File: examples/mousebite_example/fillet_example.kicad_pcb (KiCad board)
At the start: 4 copper layers, 43.2 x 30.5 mm, 0 parts

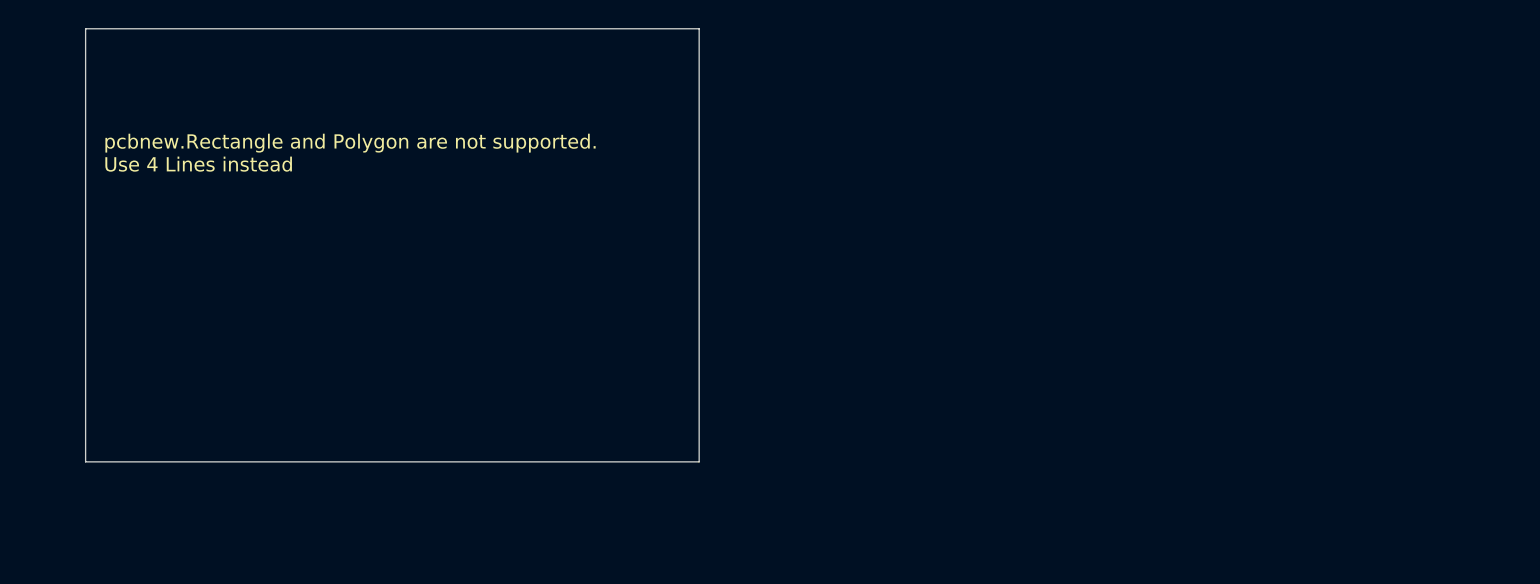
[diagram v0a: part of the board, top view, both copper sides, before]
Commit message: Mousebite better
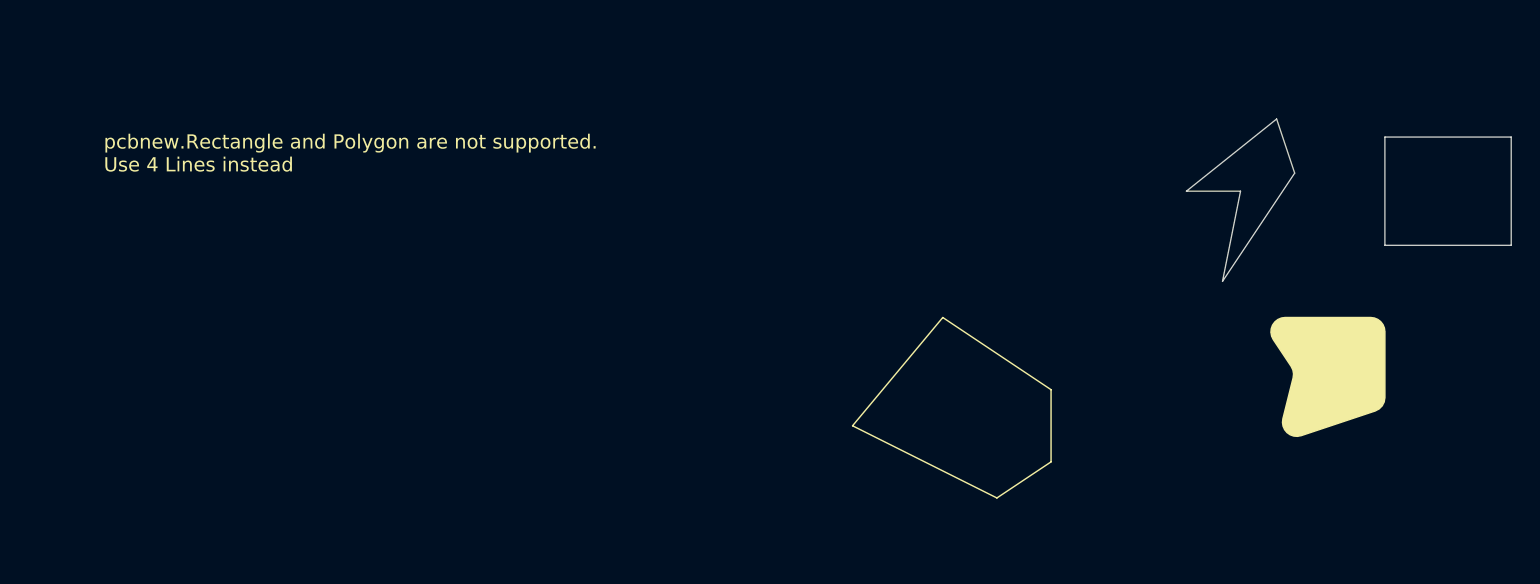
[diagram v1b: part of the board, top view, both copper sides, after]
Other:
- board size 43.2 x 30.5 mm -> 22.9 x 11.4 mm
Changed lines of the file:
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@@
   (gr_arc (start 122.866947 122.545438) (mid 122.177267 123.07704) (end 121.332335 122.866447)
+    (stroke (width 0.1) (type default)) (layer "F.SilkS"))
+  (gr_line (start 147.701 95.758) (end 147.701 100.838)
     (stroke (width 0.1) (type default)) (layer "F.SilkS"))
   (gr_line (start 150.876 121.158) (end 140.716 121.158)
@@
   (gr_line (start 50.546 135.128) (end 59.436 119.888)
     (stroke (width 0.1) (type default)) (layer "F.SilkS"))
+  (gr_poly
+    (pts
+      (xy 163.342467 92.2327)
+      (xy 163.224702 91.990813)
+      (xy 163.175683 91.726284)
+      (xy 163.198958 91.458261)
+      (xy 163.292842 91.206142)
+      (xy 163.450541 90.988175)
+      (xy 163.660639 90.820137)
+      (xy 163.90793 90.714189)
+      (xy 164.174517 90.678)
+      (xy 170.196 90.678)
+      (xy 170.454819 90.712074)
+      (xy 170.696 90.811975)
+      (xy 170.903107 90.970893)
+      (xy 171.062025 91.178)
+      (xy 171.161926 91.419181)
+      (xy 171.196 91.678)
+      (xy 171.196 96.307241)
+      (xy 171.147641 96.614452)
+      (xy 171.007242 96.891951)
+      (xy 170.788382 97.112898)
+      (xy 170.512228 97.255924)
+      (xy 165.304191 98.991936)
+      (xy 165.042496 99.041765)
+      (xy 164.776931 99.020732)
+      (xy 164.526342 98.93033)
+      (xy 164.308514 98.776975)
+      (xy 164.138903 98.57155)
+      (xy 164.029549 98.328633)
+      (xy 163.98821 98.065463)
+      (xy 164.017821 97.800717)
+      (xy 164.73871 94.917162)
+      (xy 164.768033 94.64195)
+      (xy 164.720796 94.369242)
+      (xy 164.600617 94.119926)
+    )
+    (stroke (width 0.1) (type solid)) (fill solid) (layer "F.SilkS"))
   (gr_line (start 163.576 121.158) (end 155.956 121.158)
     (stroke (width 0.1) (type default)) (layer "F.SilkS"))
@@
     (stroke (width 0.1) (type default)) (layer "F.SilkS"))
   (gr_line (start 134.366 119.888) (end 134.366 124.968)
+    (stroke (width 0.1) (type default)) (layer "F.SilkS"))
+  (gr_line (start 140.081 90.678) (end 147.701 95.758)
     (stroke (width 0.1) (type default)) (layer "F.SilkS"))
   (gr_line (start 69.596 136.398) (end 59.436 150.368)
@@
   (gr_arc (start 131.316207 125.799343) (mid 131.482224 126.291906) (end 131.378583 126.801257)
     (stroke (width 0.1) (type default)) (layer "F.SilkS"))
+  (gr_line (start 133.731 98.298) (end 140.081 90.678)
+    (stroke (width 0.1) (type default)) (layer "F.SilkS"))
   (gr_line (start 105.156 141.478) (end 97.536 135.128)
     (stroke (width 0.1) (type default)) (layer "F.SilkS"))
   (gr_line (start 59.436 132.588) (end 67.056 135.128)
     (stroke (width 0.1) (type default)) (layer "F.SilkS"))
+  (gr_line (start 143.891 103.378) (end 133.731 98.298)
+    (stroke (width 0.1) (type default)) (layer "F.SilkS"))
   (gr_line (start 94.361 135.128) (end 84.201 149.098)
+    (stroke (width 0.1) (type default)) (layer "F.SilkS"))
+  (gr_line (start 147.701 100.838) (end 143.891 103.378)
     (stroke (width 0.1) (type default)) (layer "F.SilkS"))
   (gr_line (start 105.156 137.668) (end 98.806 135.128)
@@
   (gr_line (start 106.109772 136.719316) (end 113.729772 134.179316)
     (stroke (width 0.15) (type default)) (layer "Eco2.User"))
-  (gr_rect (start 79.756 70.358) (end 122.936 100.838)
+  (gr_rect (start 171.196 77.978) (end 180.086 85.598)
     (stroke (width 0.05) (type default)) (fill none) (layer "Edge.Cuts"))
+  (gr_poly
+    (pts
+      (xy 157.226 81.788)
+      (xy 163.576 76.708)
+      (xy 164.846 80.518)
+      (xy 159.766 88.138)
+      (xy 161.036 81.788)
+    )
+    (stroke (width 0.05) (type solid)) (fill none) (layer "Edge.Cuts"))
   (gr_text "pcbnew.Rectangle and Polygon are not supported.\nUse 4 Lines instead" (at 81.026 80.518) (layer "F.SilkS")
     (effects (font (size 1 1) (thickness 0.1)) (justify left bottom))
